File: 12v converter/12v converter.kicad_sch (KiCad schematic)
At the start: 12 parts, among them U1 LM2674N-3.3

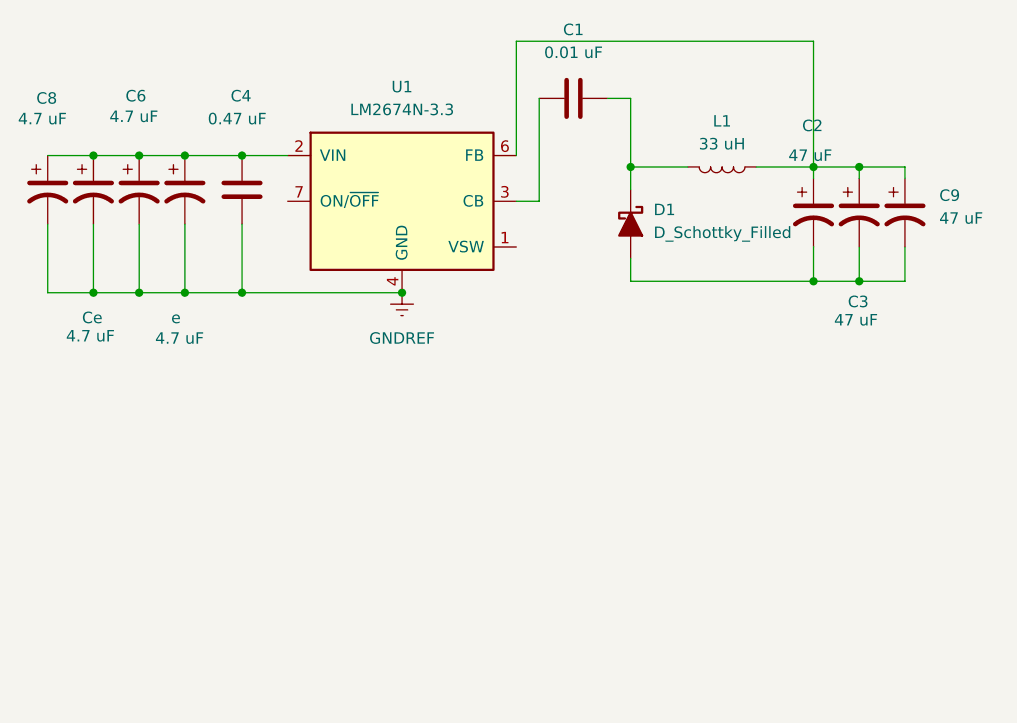
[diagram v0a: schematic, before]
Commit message: Added power flags, added J1 and J2 symbols for input and output, put no connect symbol on ON/OFF, created SW_OUT labels, fixed annotation error
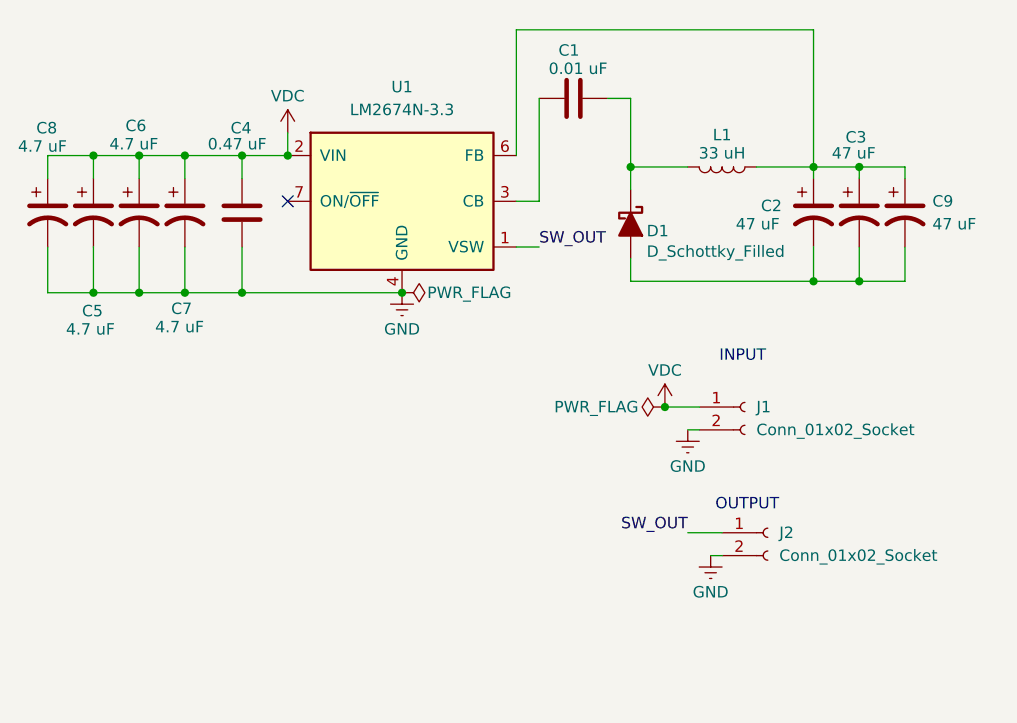
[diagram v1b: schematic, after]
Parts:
- added J1, J2: Conn_01x02_Socket, symbol Connector:Conn_01x02_Socket
- renumbered Ce to C5, e to C7
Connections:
- net VDC: now reaches C4.1, C5.1, C6.1, C7.1, C8.1, U1.2 (VIN)
- net VDC: now also J1.1 (Pin_1)
- net SW_OUT: now reaches U1.1 (VSW)
- net SW_OUT: now also J2.1 (Pin_1)
- net GNDREF renamed GND
- net GND: now also J1.2 (Pin_2), J2.2 (Pin_2)
- no-connect marks 0 -> 1
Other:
- note added: "INPUT"
- note added: "OUTPUT"
- moved on the sheet: C4, C5, C6, C7, C8

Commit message: started PCB, updated footprints for inductor and J1 and J2 in schematic
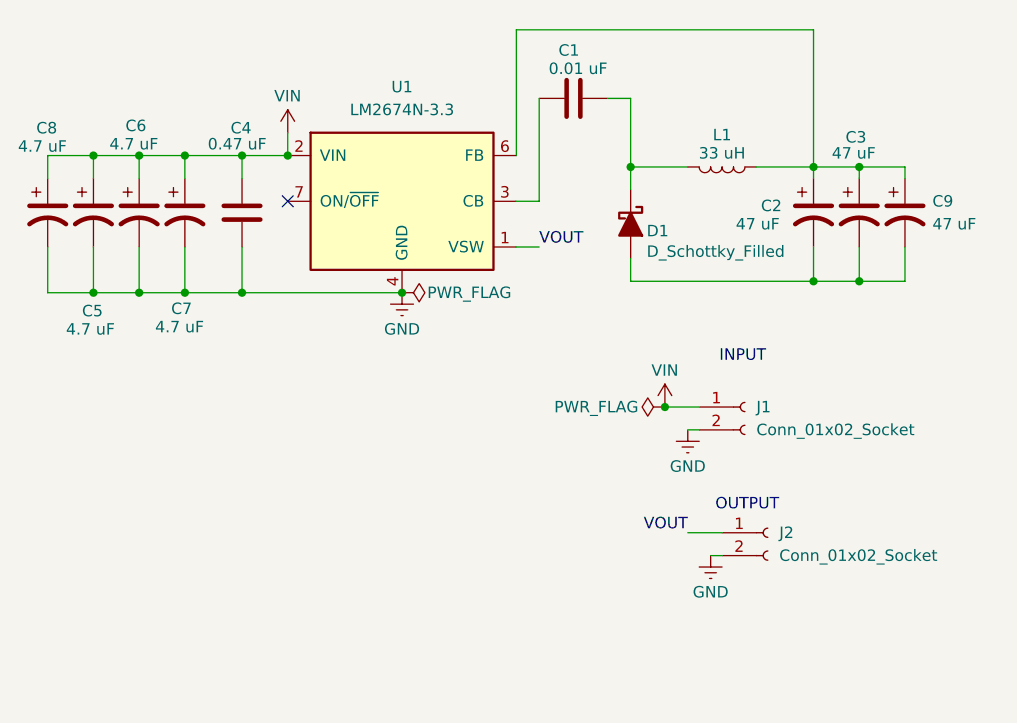
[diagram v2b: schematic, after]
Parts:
- D1: footprint Package_TO_SOT_SMD:TO-252-3_TabPin2 -> fcp12vconv_footprints:TO-252-3_TabPin2_Single
- J1, J2: footprint (none) -> fcp12vconv_footprints:PHOENIX_1777545
- L1: footprint (none) -> fcp12vconv_footprints:WE-HCI_1365
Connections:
- net SW_OUT renamed VOUT
- net VDC renamed VIN
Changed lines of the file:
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@@
 		)
 	)
-	(label "SW_OUT"
+	(label "VOUT"
 		(at 180.34 90.17 0)
 		(fields_autoplaced yes)
@@
 		)
 	)
-	(label "SW_OUT"
+	(label "VOUT"
 		(at 196.85 121.92 180)
 		(fields_autoplaced yes)
@@
 			)
 		)
-		(property "Footprint" ""
+		(property "Footprint" "fcp12vconv_footprints:PHOENIX_1777545"
 			(at 205.74 121.92 0)
 			(effects
@@
 			)
 		)
-		(property "Datasheet" "~"
+		(property "Datasheet" "https://mm.digikey.com/Volume0/opasdata/d220001/medias/docus/404/1777545.pdf"
 			(at 205.74 121.92 0)
 			(effects
@@
 			)
 		)
-		(property "Value" "VDC"
+		(property "Value" "VIN"
 			(at 152.4 73.406 0)
 			(effects
@@
 			)
 		)
-		(property "Footprint" ""
+		(property "Footprint" "fcp12vconv_footprints:WE-HCI_1365"
 			(at 200.66 81.28 0)
 			(effects
@@
 			)
 		)
-		(property "Datasheet" "https://productfinder.pulseeng.com/products/datasheets/SPM2007_46.pdf"
+		(property "Datasheet" "https://www.we-online.com/components/products/datasheet/7443551331.pdf"
 			(at 200.66 81.28 0)
 			(effects
@@
 			)
 		)
-		(property "Footprint" "Package_TO_SOT_SMD:TO-252-3_TabPin2"
+		(property "Footprint" "fcp12vconv_footprints:TO-252-3_TabPin2_Single"
 			(at 190.5 87.63 0)
 			(effects
@@
 			)
 		)
-		(property "Value" "VDC"
+		(property "Value" "VIN"
 			(at 194.31 103.886 0)
 			(effects
@@
 			)
 		)
-		(property "Footprint" ""
+		(property "Footprint" "fcp12vconv_footprints:PHOENIX_1777545"
 			(at 203.2 107.95 0)
 			(effects
@@
 			)
 		)
-		(property "Datasheet" "~"
+		(property "Datasheet" "https://mm.digikey.com/Volume0/opasdata/d220001/medias/docus/404/1777545.pdf"
 			(at 203.2 107.95 0)
 			(effects

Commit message: Completed layout. Fixed incorrect schematic connections. Converted supermileage logo to silkscreen and added to layout
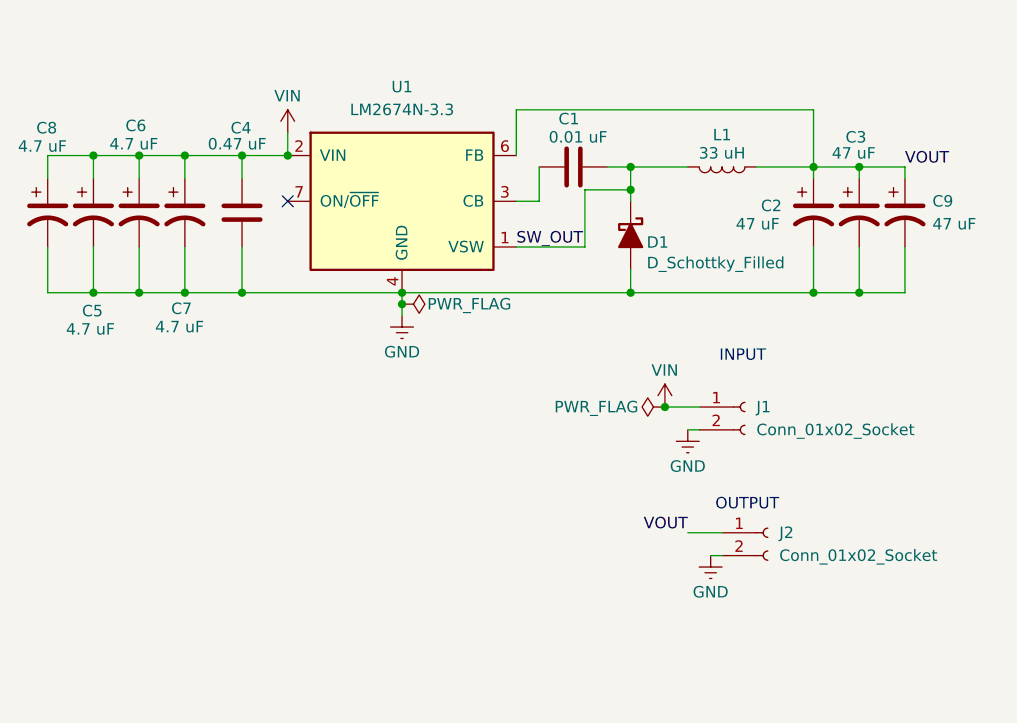
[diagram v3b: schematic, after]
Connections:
- net GND: now also C2.2, C3.2, C9.2, D1.2 (A)
- net VOUT: now also C2.1, C3.1, C9.1, L1.1, U1.6 (FB); no longer U1.1 (VSW)
- net SW_OUT: now reaches C1.2, D1.1 (K), L1.2
- net SW_OUT: now also U1.1 (VSW)
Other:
- moved on the sheet: C1, D1
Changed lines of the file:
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@@
+	)
+	(junction
+		(at 190.5 83.82)
+		(diameter 0)
+		(color 0 0 0 0)
 	)
 	(junction
@@
 	)
 	(junction
+		(at 215.9 95.25)
+		(diameter 0)
+		(color 0 0 0 0)
+	)
+	(junction
 		(at 135.89 95.25)
 		(diameter 0)
@@
 	)
 	(junction
-		(at 215.9 93.98)
+		(at 210.82 95.25)
 		(diameter 0)
 		(color 0 0 0 0)
@@
 	)
 	(junction
-		(at 210.82 93.98)
+		(at 190.5 95.25)
+		(diameter 0)
+		(color 0 0 0 0)
+	)
+	(junction
+		(at 165.1 96.52)
 		(diameter 0)
 		(color 0 0 0 0)
@@
 	(wire
 		(pts
-			(xy 210.82 93.98) (xy 210.82 90.17)
+			(xy 190.5 83.82) (xy 190.5 85.09)
 		)
 		(stroke
@@
 	(wire
 		(pts
+			(xy 165.1 96.52) (xy 165.1 95.25)
+		)
+		(stroke
+			(width 0)
+			(type default)
+		)
+	)
+	(wire
+		(pts
 			(xy 125.73 80.01) (xy 125.73 82.55)
 		)
@@
 	(wire
 		(pts
-			(xy 190.5 73.66) (xy 190.5 81.28)
-		)
-		(stroke
-			(width 0)
-			(type default)
-		)
-	)
-	(wire
-		(pts
 			(xy 130.81 90.17) (xy 130.81 95.25)
 		)
@@
 	(wire
 		(pts
+			(xy 210.82 90.17) (xy 210.82 95.25)
+		)
+		(stroke
+			(width 0)
+			(type default)
+		)
+	)
+	(wire
+		(pts
 			(xy 194.31 107.95) (xy 198.12 107.95)
 		)
@@
 	(wire
 		(pts
-			(xy 210.82 66.04) (xy 210.82 81.28)
-		)
-		(stroke
-			(width 0)
-			(type default)
-		)
-	)
-	(wire
-		(pts
-			(xy 210.82 93.98) (xy 215.9 93.98)
-		)
-		(stroke
-			(width 0)
-			(type default)
-		)
-	)
-	(wire
-		(pts
-			(xy 177.8 80.01) (xy 177.8 66.04)
-		)
-		(stroke
-			(width 0)
-			(type default)
-		)
-	)
-	(wire
-		(pts
-			(xy 190.5 91.44) (xy 190.5 93.98)
-		)
-		(stroke
-			(width 0)
-			(type default)
-		)
-	)
-	(wire
-		(pts
-			(xy 190.5 93.98) (xy 210.82 93.98)
+			(xy 185.42 83.82) (xy 185.42 90.17)
+		)
+		(stroke
+			(width 0)
+			(type default)
+		)
+	)
+	(wire
+		(pts
+			(xy 210.82 74.93) (xy 210.82 81.28)
+		)
+		(stroke
+			(width 0)
+			(type default)
+		)
+	)
+	(wire
+		(pts
+			(xy 210.82 95.25) (xy 215.9 95.25)
+		)
+		(stroke
+			(width 0)
+			(type default)
+		)
+	)
+	(wire
+		(pts
+			(xy 177.8 80.01) (xy 177.8 74.93)
+		)
+		(stroke
+			(width 0)
+			(type default)
+		)
+	)
+	(wire
+		(pts
+			(xy 165.1 96.52) (xy 165.1 97.79)
+		)
+		(stroke
+			(width 0)
+			(type default)
+		)
+	)
+	(wire
+		(pts
+			(xy 190.5 92.71) (xy 190.5 95.25)
+		)
+		(stroke
+			(width 0)
+			(type default)
+		)
+	)
+	(wire
+		(pts
+			(xy 190.5 95.25) (xy 210.82 95.25)
 		)
 		(stroke
@@
 	(wire
 		(pts
-			(xy 220.98 93.98) (xy 215.9 93.98)
+			(xy 220.98 95.25) (xy 215.9 95.25)
 		)
 		(stroke
@@
 	(wire
 		(pts
-			(xy 177.8 66.04) (xy 210.82 66.04)
+			(xy 215.9 90.17) (xy 215.9 95.25)
+		)
+		(stroke
+			(width 0)
+			(type default)
+		)
+	)
+	(wire
+		(pts
+			(xy 177.8 74.93) (xy 210.82 74.93)
+		)
+		(stroke
+			(width 0)
+			(type default)
+		)
+	)
+	(wire
+		(pts
+			(xy 165.1 95.25) (xy 190.5 95.25)
 		)
 		(stroke
@@
 	(wire
 		(pts
-			(xy 180.34 73.66) (xy 180.34 85.09)
+			(xy 180.34 81.28) (xy 180.34 85.09)
 		)
 		(stroke
@@
 	(wire
 		(pts
-			(xy 177.8 90.17) (xy 180.34 90.17)
+			(xy 177.8 90.17) (xy 185.42 90.17)
 		)
 		(stroke
@@
 	(wire
 		(pts
-			(xy 220.98 90.17) (xy 220.98 93.98)
+			(xy 220.98 90.17) (xy 220.98 95.25)
 		)
 		(stroke
@@
 	(wire
 		(pts
-			(xy 187.96 73.66) (xy 190.5 73.66)
+			(xy 187.96 81.28) (xy 190.5 81.28)
 		)
 		(stroke
@@
 	(wire
 		(pts
-			(xy 215.9 93.98) (xy 215.9 90.17)
-		)
-		(stroke
-			(width 0)
-			(type default)
-		)
-	)
-	(wire
-		(pts
 			(xy 125.73 80.01) (xy 130.81 80.01)
 		)
@@
 		(pts
 			(xy 130.81 95.25) (xy 135.89 95.25)
+		)
+		(stroke
+			(width 0)
+			(type default)
+		)
+	)
+	(wire
+		(pts
+			(xy 185.42 83.82) (xy 190.5 83.82)
 		)
 		(stroke
@@
 		)
 	)
-	(label "VOUT"
-		(at 180.34 90.17 0)
+	(label "SW_OUT"
+		(at 177.8 90.17 0)
 		(fields_autoplaced yes)
 		(effects
@@
 		)
 	)
+	(label "VOUT"
+		(at 220.98 81.28 0)
+		(fields_autoplaced yes)
+		(effects
+			(font
+				(size 1.27 1.27)
+			)
+			(justify left bottom)
+		)
+	)
 	(symbol
 		(lib_id "Device:C")
@@
 	(symbol
 		(lib_id "power:PWR_FLAG")
-		(at 165.1 95.25 270)
+		(at 165.1 96.52 270)
 		(unit 1)
 		(exclude_from_sim no)
@@
 		(dnp no)
 		(property "Reference" "#FLG01"
-			(at 167.005 95.25 0)
+			(at 167.005 96.52 0)
 			(effects
 				(font
@@
 		)
 		(property "Value" "PWR_FLAG"
-			(at 167.894 95.25 90)
+			(at 167.894 96.52 90)
 			(effects
 				(font
@@
 		)
 		(property "Footprint" ""
-			(at 165.1 95.25 0)
+			(at 165.1 96.52 0)
 			(effects
 				(font
@@
 		)
 		(property "Datasheet" "~"
-			(at 165.1 95.25 0)
+			(at 165.1 96.52 0)
 			(effects
 				(font
@@
 		)
 		(property "Description" "Special symbol for telling ERC where power comes from"
-			(at 165.1 95.25 0)
+			(at 165.1 96.52 0)
 			(effects
 				(font
@@
 	(symbol
 		(lib_id "Device:D_Schottky_Filled")
-		(at 190.5 87.63 270)
+		(at 190.5 88.9 270)
 		(unit 1)
 		(exclude_from_sim no)
@@
 		(dnp no)
 		(property "Reference" "D1"
-			(at 192.278 88.392 90)
+			(at 192.278 89.662 90)
 			(effects
 				(font
@@
 		)
 		(property "Value" "D_Schottky_Filled"
-			(at 192.278 90.678 90)
+			(at 192.278 91.948 90)
 			(effects
 				(font
@@
 		)
 		(property "Footprint" "fcp12vconv_footprints:TO-252-3_TabPin2_Single"
-			(at 190.5 87.63 0)
+			(at 190.5 88.9 0)
 			(effects
 				(font
@@
 		)
 		(property "Datasheet" "https://www.smc-diodes.com/propdf/MBRD1545CT%20N0046%20REV.A.pdf"
-			(at 190.5 87.63 0)
+			(at 190.5 88.9 0)
 			(effects
 				(font
@@
 		)
 		(property "Description" "Schottky diode, filled shape"
-			(at 190.5 87.63 0)
+			(at 190.5 88.9 0)
 			(effects
 				(font
@@
 	(symbol
 		(lib_id "Device:C")
-		(at 184.15 73.66 90)
+		(at 184.15 81.28 90)
 		(unit 1)
 		(exclude_from_sim no)
@@
 		(dnp no)
 		(property "Reference" "C1"
-			(at 183.642 68.326 90)
+			(at 183.642 75.946 90)
 			(effects
 				(font
@@
 		)
 		(property "Value" "0.01 uF"
-			(at 184.658 70.358 90)
+			(at 184.658 77.978 90)
 			(effects
 				(font
@@
 		)
 		(property "Footprint" "Capacitor_SMD:C_0603_1608Metric_Pad1.08x0.95mm_HandSolder"
-			(at 187.96 72.6948 0)
+			(at 187.96 80.3148 0)
 			(effects
 				(font
@@
 		)
 		(property "Datasheet" "https://search.kemet.com/download/datasheet/C0603C103K5RAC7867"
-			(at 184.15 73.66 0)
+			(at 184.15 81.28 0)
 			(effects
 				(font
@@
 		)
 		(property "Description" "Unpolarized capacitor"
-			(at 184.15 73.66 0)
+			(at 184.15 81.28 0)
 			(effects
 				(font
@@
 	(symbol
 		(lib_id "power:GNDREF")
-		(at 165.1 95.25 0)
+		(at 165.1 97.79 0)
 		(unit 1)
 		(exclude_from_sim no)
@@
 		(dnp no)
 		(property "Reference" "#PWR01"
-			(at 165.1 101.6 0)
+			(at 165.1 104.14 0)
 			(effects
 				(font
@@
 		)
 		(property "Value" "GND"
-			(at 165.1 99.314 0)
+			(at 165.1 101.854 0)
 			(effects
 				(font
@@
 		)
 		(property "Footprint" ""
-			(at 165.1 95.25 0)
+			(at 165.1 97.79 0)
 			(effects
 				(font
@@
 		)
 		(property "Datasheet" ""
-			(at 165.1 95.25 0)
+			(at 165.1 97.79 0)
 			(effects
 				(font
@@
 		)
 		(property "Description" "Power symbol creates a global label with name \"GNDREF\" , reference supply ground"
-			(at 165.1 95.25 0)
-			(effects
-				(font
+			(at 165.1 97.79 0)
+			(effects
+				(font

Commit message: test points, labels
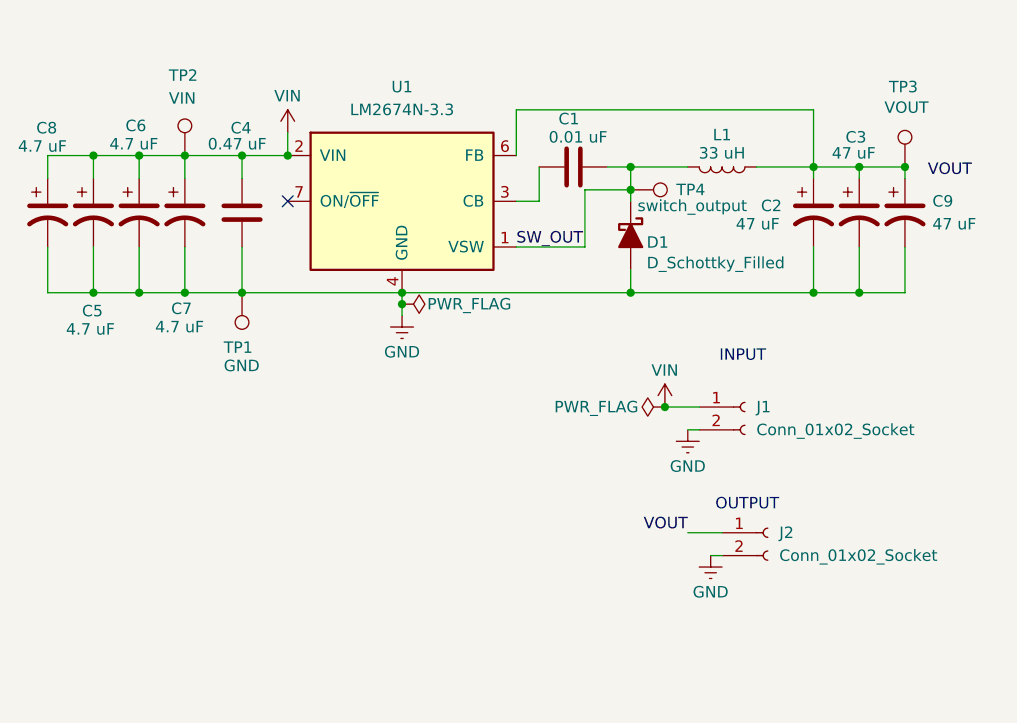
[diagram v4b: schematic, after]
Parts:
- added TP1: GND, TestPoint:TestPoint_Pad_1.0x1.0mm, symbol Connector:TestPoint
- added TP2: VIN, TestPoint:TestPoint_Pad_1.0x1.0mm, symbol Connector:TestPoint
- added TP3: VOUT, TestPoint:TestPoint_Pad_1.0x1.0mm, symbol Connector:TestPoint
- added TP4: switch_output, TestPoint:TestPoint_Pad_1.0x1.0mm, symbol Connector:TestPoint
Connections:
- net GND: now also TP1.1
- net SW_OUT: now also TP4.1
- net VIN: now also TP2.1
- net VOUT: no longer C2.1, C3.1, C9.1, L1.1, U1.6 (FB)
- new net: C2.1, C3.1, C9.1, L1.1, TP3.1, U1.6 (FB)

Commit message: rearrangmenet, silkscreen stuff
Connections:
- net VOUT: now also C2.1, C3.1, C9.1, L1.1, TP3.1, U1.6 (FB)
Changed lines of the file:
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@@
 	)
 	(label "VOUT"
-		(at 223.52 82.55 0)
+		(at 220.98 81.28 0)
 		(fields_autoplaced yes)
 		(effects

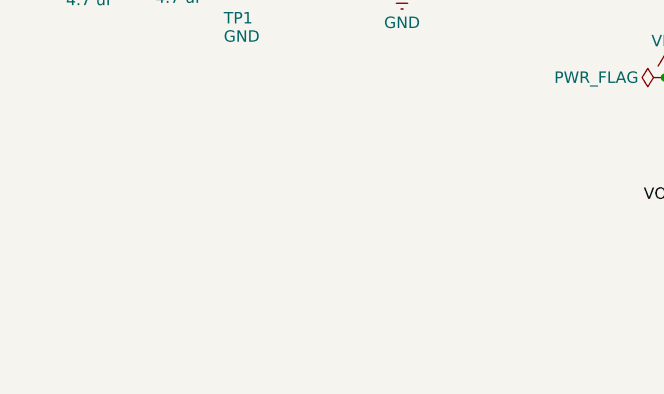
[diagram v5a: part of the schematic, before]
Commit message: Fixed silkscreen RefDes labels, made component values visible, added mounting holes with keepout zones around them. Generated gerber, drill and drill map files
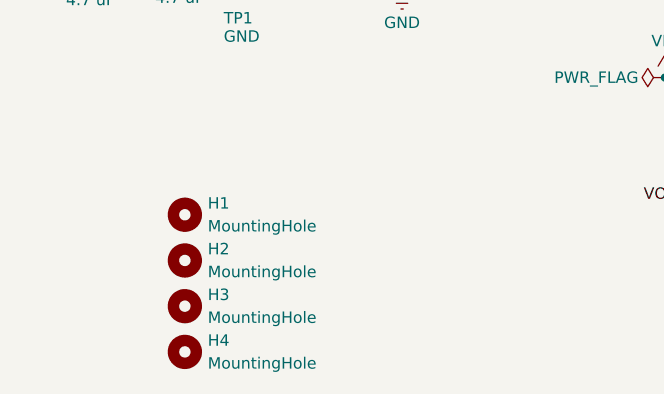
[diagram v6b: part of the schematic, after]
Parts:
- added H1, H2, H3, H4: MountingHole, MountingHole:MountingHole_2.2mm_M2, symbol Mechanical:MountingHole

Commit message: changed D1 footprint from TO-252-3 to TO-252 then altered it (only on board) to make the outer pins GND and the pad SW_OUT
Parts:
- D1: footprint fcp12vconv_footprints:TO-252-3_TabPin2_Single -> Package_TO_SOT_SMD:TO-252-2
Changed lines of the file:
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@@
 			)
 		)
-		(property "Footprint" "fcp12vconv_footprints:TO-252-3_TabPin2_Single"
+		(property "Footprint" "Package_TO_SOT_SMD:TO-252-2"
 			(at 190.5 88.9 0)
 			(effects
